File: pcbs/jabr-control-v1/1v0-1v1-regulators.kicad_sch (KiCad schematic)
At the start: 22 parts, among them U1501 TPS62290TDRVRQ1, U3801 TPS62290TDRVRQ1

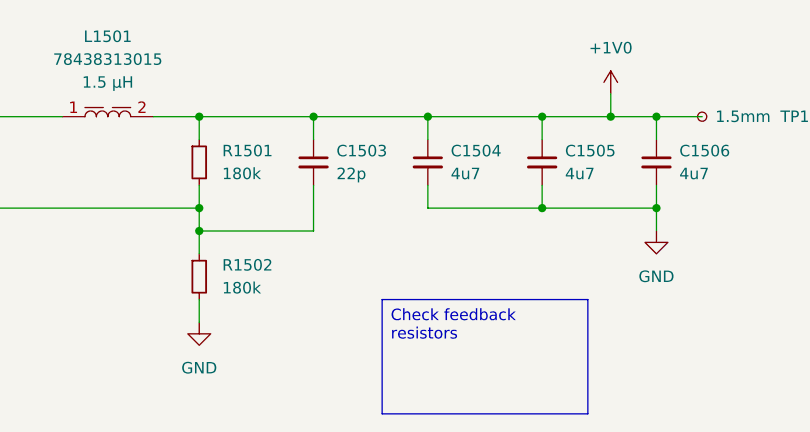
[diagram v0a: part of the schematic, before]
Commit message: Updated 1v0 regulator feedback resistors
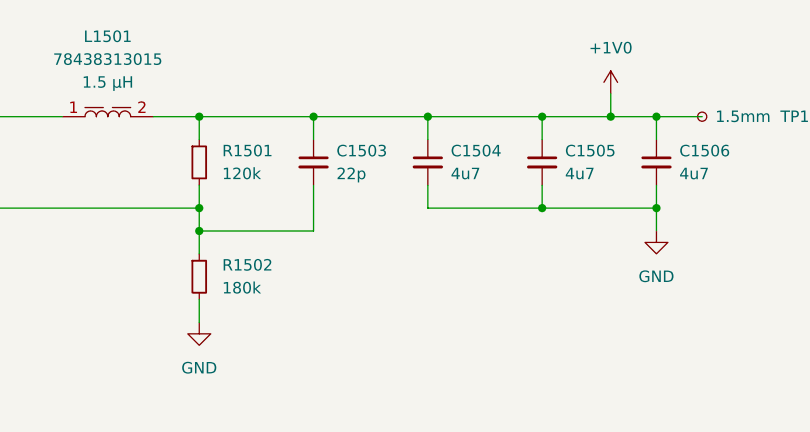
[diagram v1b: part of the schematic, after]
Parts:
- R1501: value 180k -> 120k
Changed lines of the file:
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@@
-		)
-	)
-	(text_box "Check feedback resistors"
-		(exclude_from_sim no)
-		(at 187.96 142.24 0)
-		(size 22.86 12.7)
-		(margins 0.9525 0.9525 0.9525 0.9525)
-		(stroke
-			(width 0)
-			(type solid)
-			(color 255 0 0 1)
-		)
-		(fill
-			(type none)
-		)
-		(effects
-			(font
-				(size 1.27 1.27)
-				(color 255 0 0 1)
-			)
-			(justify left top)
 		)
 	)
@@
 			)
 		)
-		(property "Value" "180k"
+		(property "Value" "120k"
 			(at 170.18 128.2699 0)
 			(effects

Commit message: Various small updates
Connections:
- net +5V: now reaches C1501.1, C1502.1, U1501.4 (EN), U1501.5 (VIN)
- net +5V: now also C3801.1, C3802.1, U3801.4 (EN), U3801.5 (VIN)
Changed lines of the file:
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@@
+	)
+	(junction
+		(at 78.74 121.92)
+		(diameter 0)
+		(color 0 0 0 0)
 	)
 	(junction
@@
 	)
 	(junction
+		(at 78.74 60.96)
+		(diameter 0)
+		(color 0 0 0 0)
+	)
+	(junction
 		(at 91.44 60.96)
 		(diameter 0)
@@
 	(wire
 		(pts
+			(xy 78.74 58.42) (xy 78.74 60.96)
+		)
+		(stroke
+			(width 0)
+			(type default)
+		)
+	)
+	(wire
+		(pts
 			(xy 167.64 132.08) (xy 167.64 134.62)
 		)
@@
 		(pts
 			(xy 78.74 121.92) (xy 78.74 124.46)
+		)
+		(stroke
+			(width 0)
+			(type default)
+		)
+	)
+	(wire
+		(pts
+			(xy 78.74 119.38) (xy 78.74 121.92)
 		)
 		(stroke
@@
 					(unit 1)
 				)
+			)
+		)
+	)
+	(symbol
+		(lib_id "power:+5V")
+		(at 78.74 119.38 0)
+		(unit 1)
+		(exclude_from_sim no)
+		(in_bom yes)
+		(on_board yes)
+		(dnp no)
+		(fields_autoplaced yes)
+		(property "Reference" "#PWR015002"
+			(at 78.74 123.19 0)
+			(effects
+				(font
+					(size 1.27 1.27)
+				)
+				(hide yes)
+			)
+		)
+		(property "Value" "+5V"
+			(at 78.74 114.3 0)
+			(effects
+				(font
+					(size 1.27 1.27)
+				)
+			)
+		)
+		(property "Footprint" ""
+			(at 78.74 119.38 0)
+			(effects
+				(font
+					(size 1.27 1.27)
+				)
+				(hide yes)
+			)
+		)
+		(property "Datasheet" ""
+			(at 78.74 119.38 0)
+			(effects
+				(font
+					(size 1.27 1.27)
+				)
+				(hide yes)
+			)
+		)
+		(property "Description" "Power symbol creates a global label with name \"+5V\""
+			(at 78.74 119.38 0)
+			(effects
+				(font
+					(size 1.27 1.27)
+				)
+				(hide yes)
+			)
+		)
+		(pin "1"
+		)
+		(instances
+			(project "jabr-control-v1"
+				(path "/f91ec272-d09a-4038-bbbb-962739a92c51/3f551047-3bb0-4f63-99e0-34fd9061d844/313ad2b1-6281-4d61-a8a6-55e55641e36c"
+					(reference "#PWR015002")
+					(unit 1)
+				)
+			)
+		)
+	)
+	(symbol
+		(lib_id "power:+5V")
+		(at 78.74 58.42 0)
+		(unit 1)
+		(exclude_from_sim no)
+		(in_bom yes)
+		(on_board yes)
+		(dnp no)
+		(fields_autoplaced yes)
+		(property "Reference" "#PWR015001"
+			(at 78.74 62.23 0)
+			(effects
+				(font
+					(size 1.27 1.27)
+				)
+				(hide yes)
+			)
+		)
+		(property "Value" "+5V"
+			(at 78.74 53.34 0)
+			(effects
+				(font
+					(size 1.27 1.27)
+				)
+			)
+		)
+		(property "Footprint" ""
+			(at 78.74 58.42 0)
+			(effects
+				(font
+					(size 1.27 1.27)
+				)
+				(hide yes)
+			)
+		)
+		(property "Datasheet" ""
+			(at 78.74 58.42 0)
+			(effects
+				(font
+					(size 1.27 1.27)
+				)
+				(hide yes)
+			)
+		)
+		(property "Description" "Power symbol creates a global label with name \"+5V\""
+			(at 78.74 58.42 0)
+			(effects
+				(font
+					(size 1.27 1.27)
+				)
+				(hide yes)
+			)
+		)
+		(pin "1"
+		)
+		(instances
+			(project "jabr-control-v1"
+				(path "/f91ec272-d09a-4038-bbbb-962739a92c51/3f551047-3bb0-4f63-99e0-34fd9061d844/313ad2b1-6281-4d61-a8a6-55e55641e36c"
+					(reference "#PWR015001")
+					(unit 1)
+				)

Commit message: Schematic nearing completion, need to do GPIO and PHY decouplings caps
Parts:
- C1501, C1502, C1503, C1504, C1505, C1506, C3801, C3802, C3804, C3805, C3806, C3807: symbol Device:C_Small -> DEV:C_SMALL
- TP1501, TP3801: footprint TestPoint:TestPoint_Pad_D1.5mm -> project_footprints:TestPoint_Pad_D1.5mm
